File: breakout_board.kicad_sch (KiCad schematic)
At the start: 0 parts

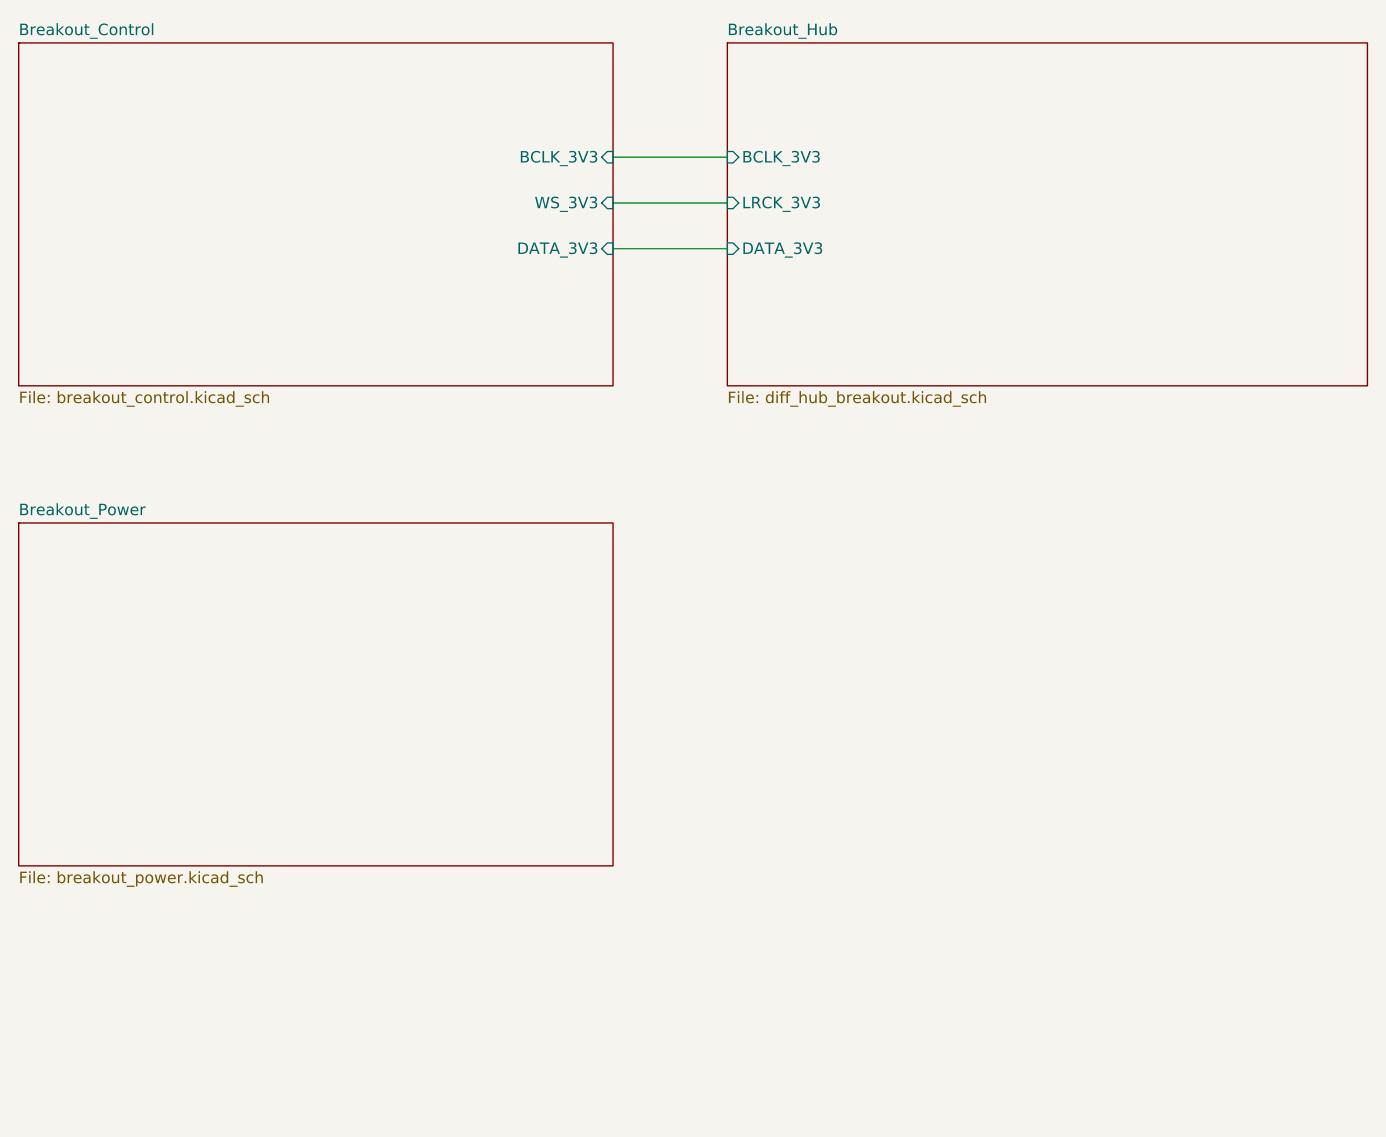
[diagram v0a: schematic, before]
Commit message: Fixed most ERC checks
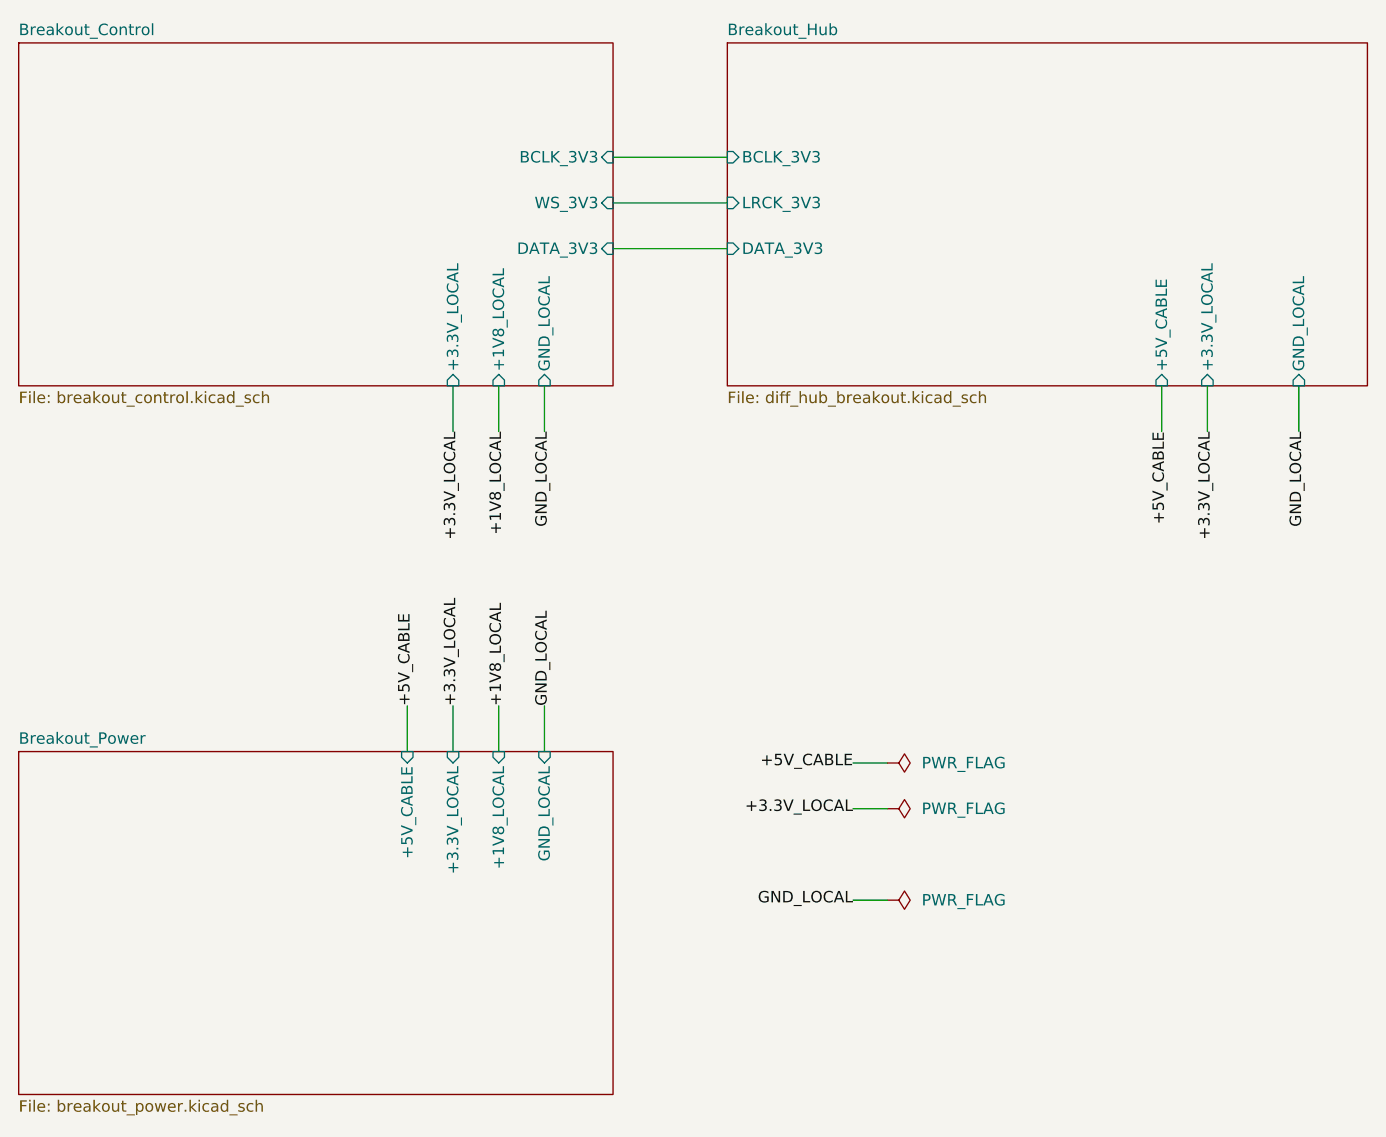
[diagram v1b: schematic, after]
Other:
- sheet Breakout_Control ports: added +1V8_LOCAL, +3.3V_LOCAL, GND_LOCAL; removed none
- sheet Breakout_Hub ports: added +3.3V_LOCAL, +5V_CABLE, GND_LOCAL; removed none
- sheet Breakout_Power ports: added +1V8_LOCAL, +3.3V_LOCAL, +5V_CABLE, GND_LOCAL; removed none
